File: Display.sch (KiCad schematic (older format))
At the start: 3 parts

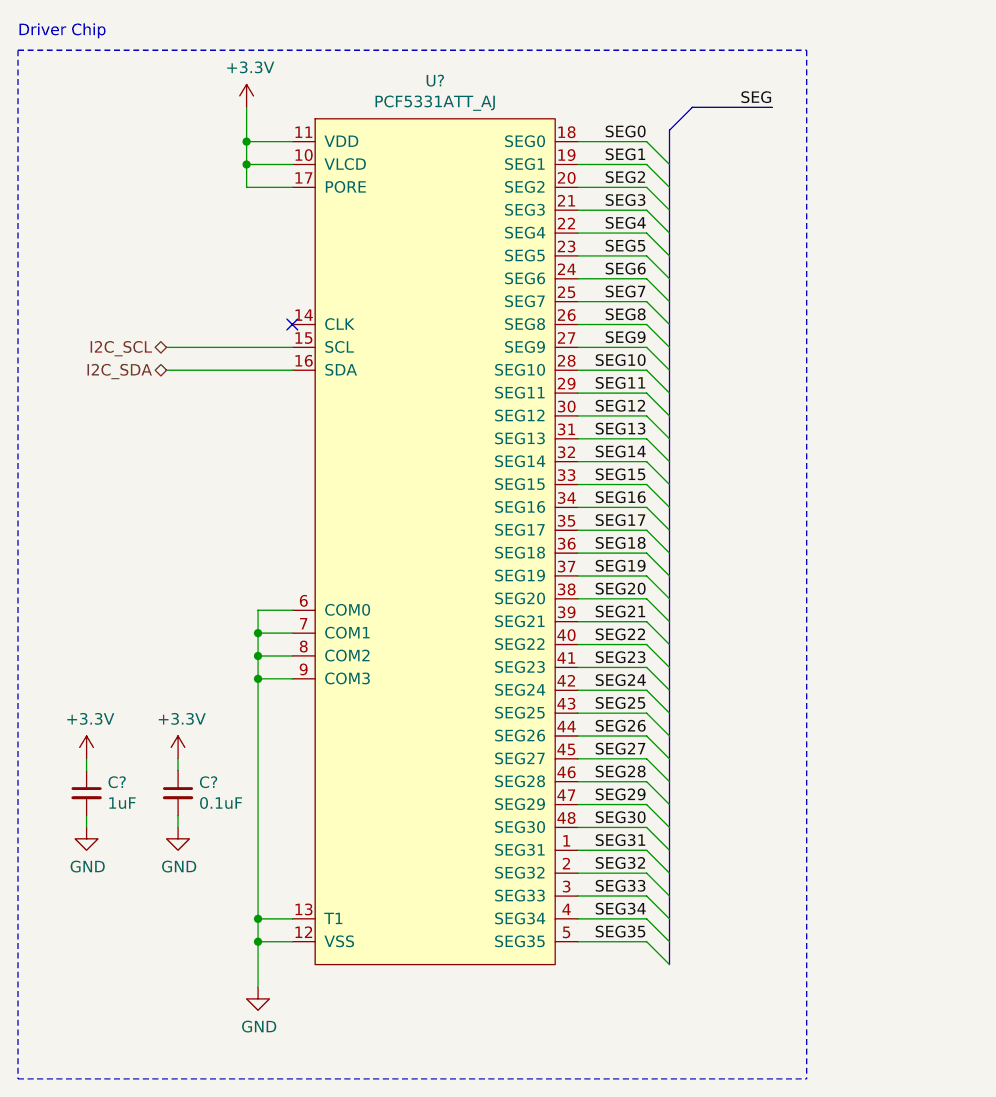
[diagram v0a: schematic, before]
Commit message: Added display driver
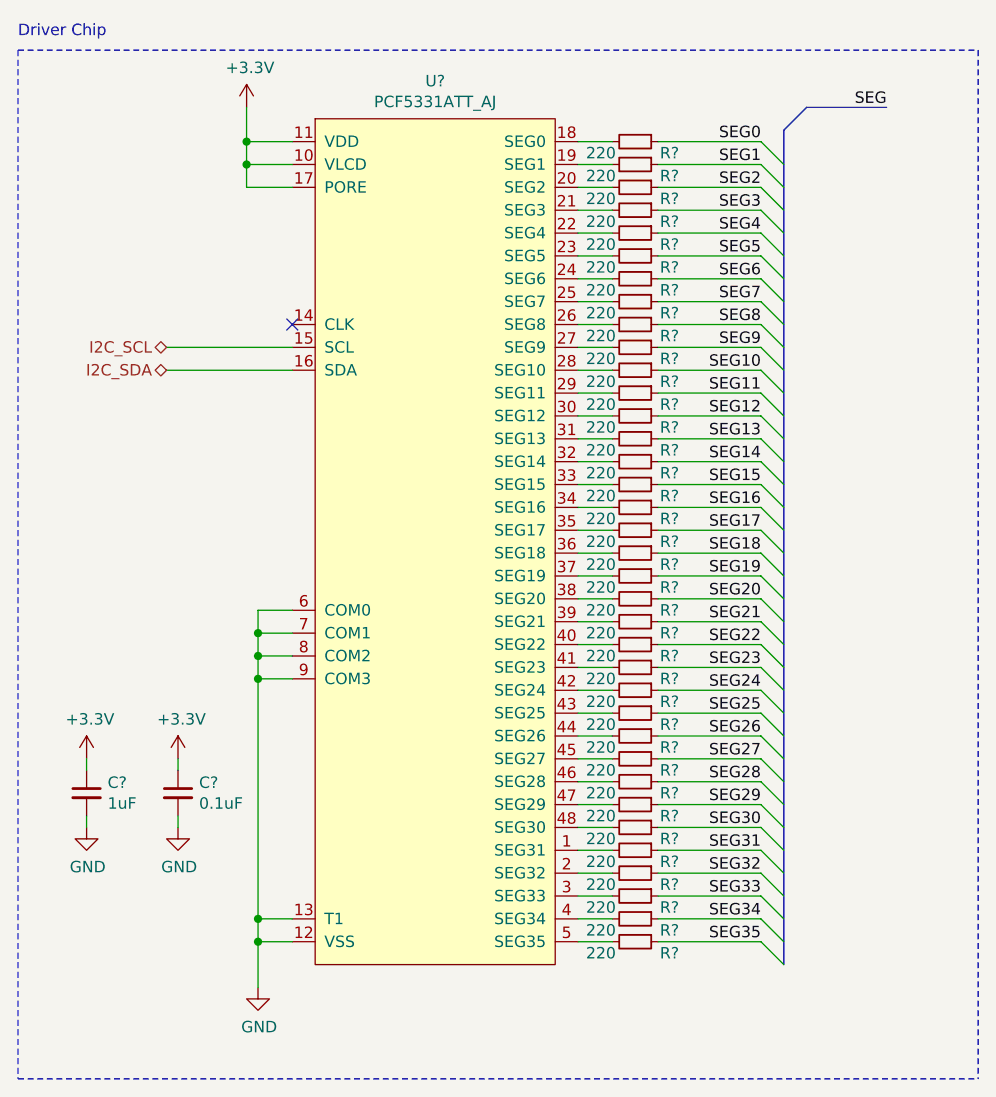
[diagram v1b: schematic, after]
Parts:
- added R? (x36): 220, symbol Device:R_Small
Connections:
- net SEG0: now also R?.1; no longer U?.18 (SEG0)
- net SEG1: now also R?.1; no longer U?.19 (SEG1)
- net SEG10: now also R?.1; no longer U?.28 (SEG10)
- net SEG11: now also R?.1; no longer U?.29 (SEG11)
- net SEG12: now also R?.1; no longer U?.30 (SEG12)
- net SEG13: now also R?.1; no longer U?.31 (SEG13)
- net SEG14: now also R?.1; no longer U?.32 (SEG14)
- net SEG15: now also R?.1; no longer U?.33 (SEG15)
- net SEG16: now also R?.1; no longer U?.34 (SEG16)
- net SEG17: now also R?.1; no longer U?.35 (SEG17)
- net SEG18: now also R?.1; no longer U?.36 (SEG18)
- net SEG19: now also R?.1; no longer U?.37 (SEG19)
- net SEG2: now also R?.1; no longer U?.20 (SEG2)
- net SEG20: now also R?.1; no longer U?.38 (SEG20)
- net SEG21: now also R?.1; no longer U?.39 (SEG21)
- net SEG22: now also R?.1; no longer U?.40 (SEG22)
- net SEG23: now also R?.1; no longer U?.41 (SEG23)
- net SEG24: now also R?.1; no longer U?.42 (SEG24)
- net SEG25: now also R?.1; no longer U?.43 (SEG25)
- net SEG26: now also R?.1; no longer U?.44 (SEG26)
- net SEG27: now also R?.1; no longer U?.45 (SEG27)
- net SEG28: now also R?.1; no longer U?.46 (SEG28)
- net SEG29: now also R?.1; no longer U?.47 (SEG29)
- net SEG3: now also R?.1; no longer U?.21 (SEG3)
- net SEG30: now also R?.1; no longer U?.48 (SEG30)
- net SEG31: now also R?.1; no longer U?.1 (SEG31)
- net SEG32: now also R?.1; no longer U?.2 (SEG32)
- net SEG33: now also R?.1; no longer U?.3 (SEG33)
- net SEG34: now also R?.1; no longer U?.4 (SEG34)
- net SEG35: now also R?.1; no longer U?.5 (SEG35)
- net SEG4: now also R?.1; no longer U?.22 (SEG4)
- net SEG5: now also R?.1; no longer U?.23 (SEG5)
- net SEG6: now also R?.1; no longer U?.24 (SEG6)
- net SEG7: now also R?.1; no longer U?.25 (SEG7)
- net SEG8: now also R?.1; no longer U?.26 (SEG8)
- net SEG9: now also R?.1; no longer U?.27 (SEG9)
- new net: R?.2, U?.1 (SEG31)
- new net: R?.2, U?.18 (SEG0)
- new net: R?.2, U?.19 (SEG1)
- new net: R?.2, U?.2 (SEG32)
- new net: R?.2, U?.20 (SEG2)
- new net: R?.2, U?.21 (SEG3)
- new net: R?.2, U?.22 (SEG4)
- new net: R?.2, U?.23 (SEG5)
- new net: R?.2, U?.24 (SEG6)
- new net: R?.2, U?.25 (SEG7)
- new net: R?.2, U?.26 (SEG8)
- new net: R?.2, U?.27 (SEG9)
- new net: R?.2, U?.28 (SEG10)
- new net: R?.2, U?.29 (SEG11)
- new net: R?.2, U?.3 (SEG33)
- new net: R?.2, U?.30 (SEG12)
- new net: R?.2, U?.31 (SEG13)
- new net: R?.2, U?.32 (SEG14)
- new net: R?.2, U?.33 (SEG15)
- new net: R?.2, U?.34 (SEG16)
- new net: R?.2, U?.35 (SEG17)
- new net: R?.2, U?.36 (SEG18)
- new net: R?.2, U?.37 (SEG19)
- new net: R?.2, U?.38 (SEG20)
- new net: R?.2, U?.39 (SEG21)
- new net: R?.2, U?.4 (SEG34)
- new net: R?.2, U?.40 (SEG22)
- new net: R?.2, U?.41 (SEG23)
- new net: R?.2, U?.42 (SEG24)
- new net: R?.2, U?.43 (SEG25)
- new net: R?.2, U?.44 (SEG26)
- new net: R?.2, U?.45 (SEG27)
- new net: R?.2, U?.46 (SEG28)
- new net: R?.2, U?.47 (SEG29)
- new net: R?.2, U?.48 (SEG30)
- new net: R?.2, U?.5 (SEG35)

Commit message: Done with preliminary schematic. Needs review
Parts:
- removed R? (x20): 220, symbol Device:R_Small
- added SEG301, SEG302, SEG303, SEG304: 7-Segment-CC, symbol ReflowOven:7-Segment-CC
- C301, C302: renamed from C?; footprint (none) -> Capacitor_SMD:C_0603_1608Metric
- R301, R302, R303, R304, R305, R306, R307, R308, R309, R310, R311, R312, R313, R314, R315, R316: renamed from R?; footprint (none) -> Resistor_SMD:R_0603_1608Metric
- gave numbers to parts that had none: 1
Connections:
- net GND: no longer U301.6 (COM0), U301.7 (COM1), U301.8 (COM2), U301.9 (COM3)
- net SEG0: now also SEG302.10 (A), SEG303.10 (A)
- net SEG1: now also SEG302.9 (B), SEG303.9 (B)
- net SEG10: now also SEG301.8 (C), SEG304.8 (C)
- net SEG11: now also SEG301.5 (D), SEG304.5 (D)
- net SEG12: now also SEG301.4 (E), SEG304.4 (E)
- net SEG13: now also SEG301.2 (F), SEG304.2 (F)
- net SEG14: now also SEG301.3 (G), SEG304.3 (G)
- net SEG15: now also SEG301.7 (DP), SEG304.7 (DP)
- net SEG2: now also SEG302.8 (C), SEG303.8 (C)
- net SEG3: now also SEG302.5 (D), SEG303.5 (D)
- net SEG4: now also SEG302.4 (E), SEG303.4 (E)
- net SEG5: now also SEG302.2 (F), SEG303.2 (F)
- net SEG6: now also SEG302.3 (G), SEG303.3 (G)
- net SEG7: now also SEG302.7 (DP), SEG303.7 (DP)
- net SEG8: now also SEG301.10 (A), SEG304.10 (A)
- net SEG9: now also SEG301.9 (B), SEG304.9 (B)
- new net COM0: SEG301.1 (CC), SEG301.6 (CC), SEG302.1 (CC), SEG302.6 (CC), U301.6 (COM0)
- new net COM1: SEG303.1 (CC), SEG303.6 (CC), SEG304.1 (CC), SEG304.6 (CC), U301.7 (COM1)
- new net COM2: U301.8 (COM2)
- new net COM3: U301.9 (COM3)
- no-connect marks 1 -> 21
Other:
- note added: "Segments"
- moved on the sheet: C301, C302, R301, R302, R303, R304, R305, R306, R307, R308, R309, R310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

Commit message: Added stuff
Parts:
- U301: footprint (none) -> Package_SO:TSSOP-48_6.1x12.5mm_P0.5mm
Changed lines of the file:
@@
 F 0 "U301" H 2375 4515 50  0000 C CNN
 F 1 "PCF5331ATT_AJ" H 2375 4424 50  0000 C CNN
-F 2 "" H 2200 4100 50  0001 C CNN
+F 2 "Package_SO:TSSOP-48_6.1x12.5mm_P0.5mm" H 2200 4100 50  0001 C CNN
 F 3 "" H 2200 4100 50  0001 C CNN
 	1    2350 2650
@@
 NoConn ~ 3000 4450
 NoConn ~ 3000 4550
+Entry Wire Line
+	3800 2550 3900 2650
 Wire Bus Line
 	5700 1100 5700 1900
@@
 Wire Bus Line
 	3900 1000 3900 2650
-Entry Wire Line
-	3800 2550 3900 2650
 $EndSCHEMATC

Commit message: Done with footprints
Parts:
- SEG301, SEG302, SEG303, SEG304: footprint (none) -> Display_7Segment:Sx39-1xxxxx
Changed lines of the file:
@@
 F 0 "SEG302" H 6550 2367 50  0000 C CNN
 F 1 "7-Segment-CC" H 6550 2276 50  0000 C CNN
-F 2 "" H 7200 1750 50  0001 C CNN
+F 2 "Display_7Segment:Sx39-1xxxxx" H 7200 1750 50  0001 C CNN
 F 3 "" H 7200 1750 50  0001 C CNN
 	1    6500 1650
@@
 F 0 "SEG303" H 6550 3817 50  0000 C CNN
 F 1 "7-Segment-CC" H 6550 3726 50  0000 C CNN
-F 2 "" H 7200 3200 50  0001 C CNN
+F 2 "Display_7Segment:Sx39-1xxxxx" H 7200 3200 50  0001 C CNN
 F 3 "" H 7200 3200 50  0001 C CNN
 	1    6500 3100
@@
 F 0 "SEG301" H 9050 2317 50  0000 C CNN
 F 1 "7-Segment-CC" H 9050 2226 50  0000 C CNN
-F 2 "" H 9700 1700 50  0001 C CNN
+F 2 "Display_7Segment:Sx39-1xxxxx" H 9700 1700 50  0001 C CNN
 F 3 "" H 9700 1700 50  0001 C CNN
 	1    9000 1600
@@
 F 0 "SEG304" H 9050 3817 50  0000 C CNN
 F 1 "7-Segment-CC" H 9050 3726 50  0000 C CNN
-F 2 "" H 9700 3200 50  0001 C CNN
+F 2 "Display_7Segment:Sx39-1xxxxx" H 9700 3200 50  0001 C CNN
 F 3 "" H 9700 3200 50  0001 C CNN
 	1    9000 3100
